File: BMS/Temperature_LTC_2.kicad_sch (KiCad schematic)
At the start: 35 parts, among them J15 Harwin M80-8542042

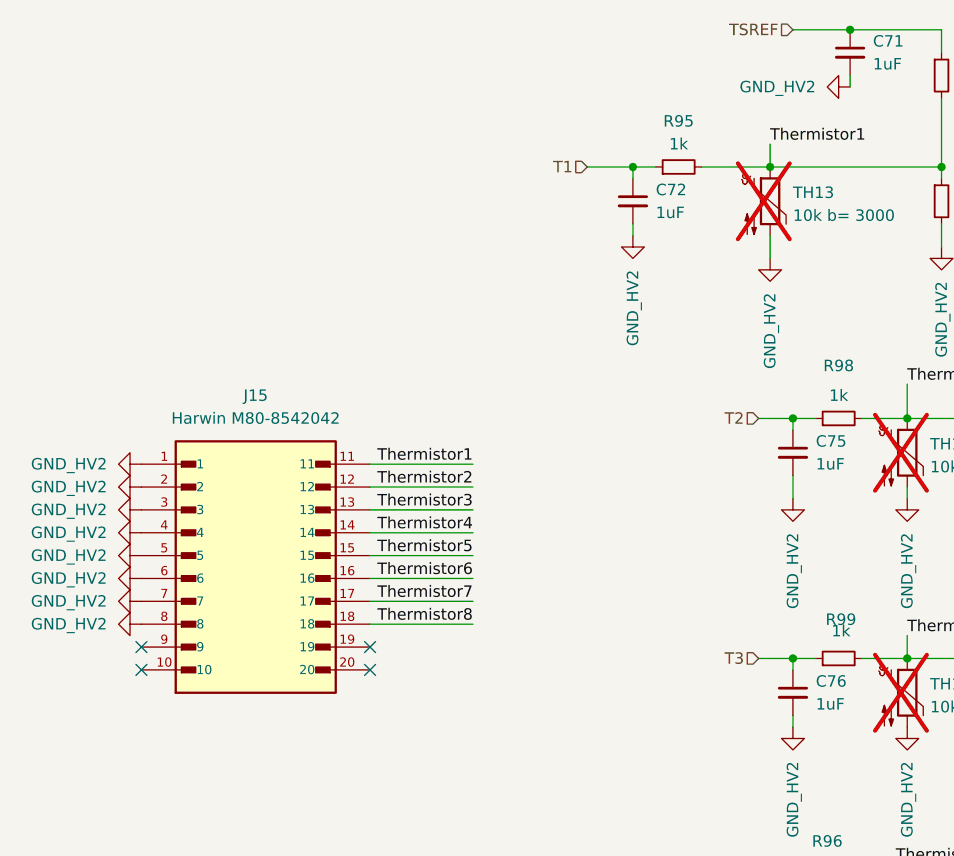
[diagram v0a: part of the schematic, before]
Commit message: Dodano layout drugiego bq79614, ukladu tlumaczącego z protokułu TI na UART oraz wstępnie poprowadzono pary różnicowe
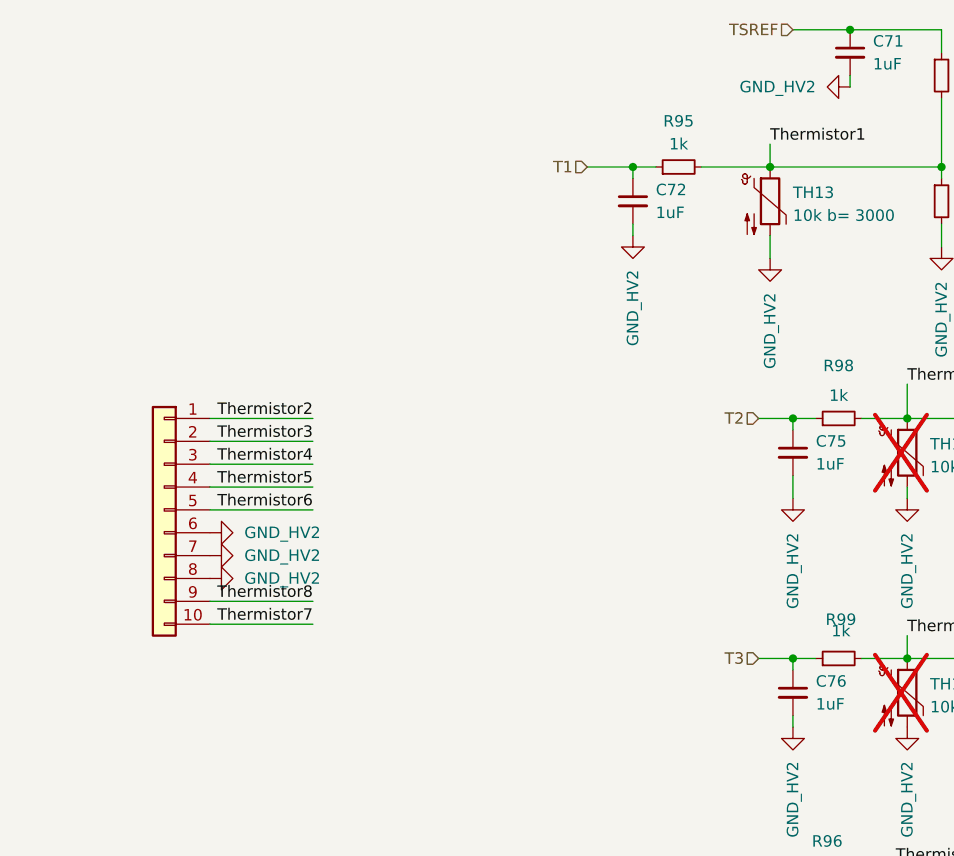
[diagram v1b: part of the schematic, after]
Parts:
- removed J15: Harwin M80-8542042, footrpint:HARWIN_M80-8542042, symbol M80-8542042:M80-8542042
- added J10: Conn_01x10, footrpint:HARWIN_G125-MV11005L1P, symbol Connector_Generic:Conn_01x10
- TH13: footprint (none) -> Resistor_SMD:R_0603_1608Metric_Pad0.98x0.95mm_HandSolder; now fitted; now in the parts list
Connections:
- net GND_HV2: now also J10.6 (Pin_6), J10.7 (Pin_7), J10.8 (Pin_8)
- net Thermistor2: now also J10.1 (Pin_1)
- net Thermistor3: now also J10.2 (Pin_2)
- net Thermistor4: now also J10.3 (Pin_3)
- net Thermistor5: now also J10.4 (Pin_4)
- net Thermistor6: now also J10.5 (Pin_5)
- net Thermistor7: now also J10.10 (Pin_10)
- net Thermistor8: now also J10.9 (Pin_9)
- no-connect marks 4 -> 0

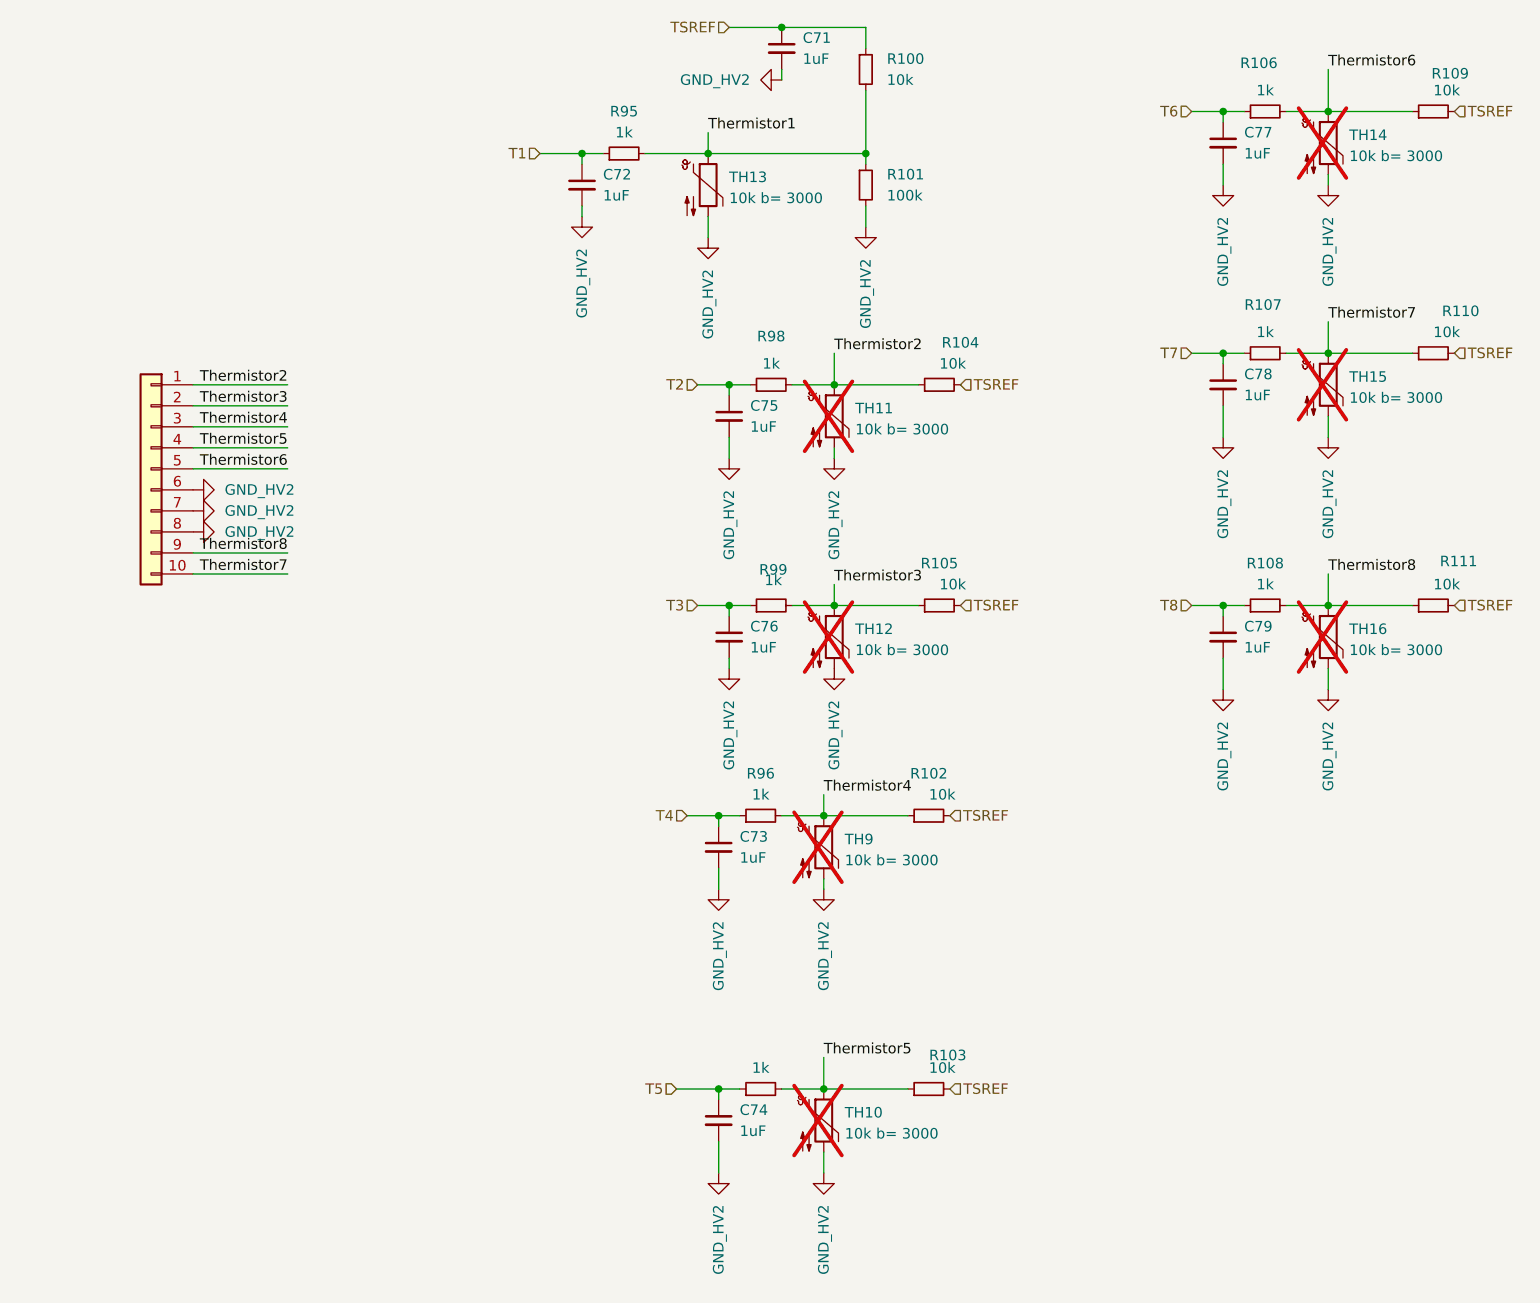
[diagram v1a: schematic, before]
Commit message: Iteracja 1.0 gotowa, teraz sprawdzenie i zmiany kosmetyczne
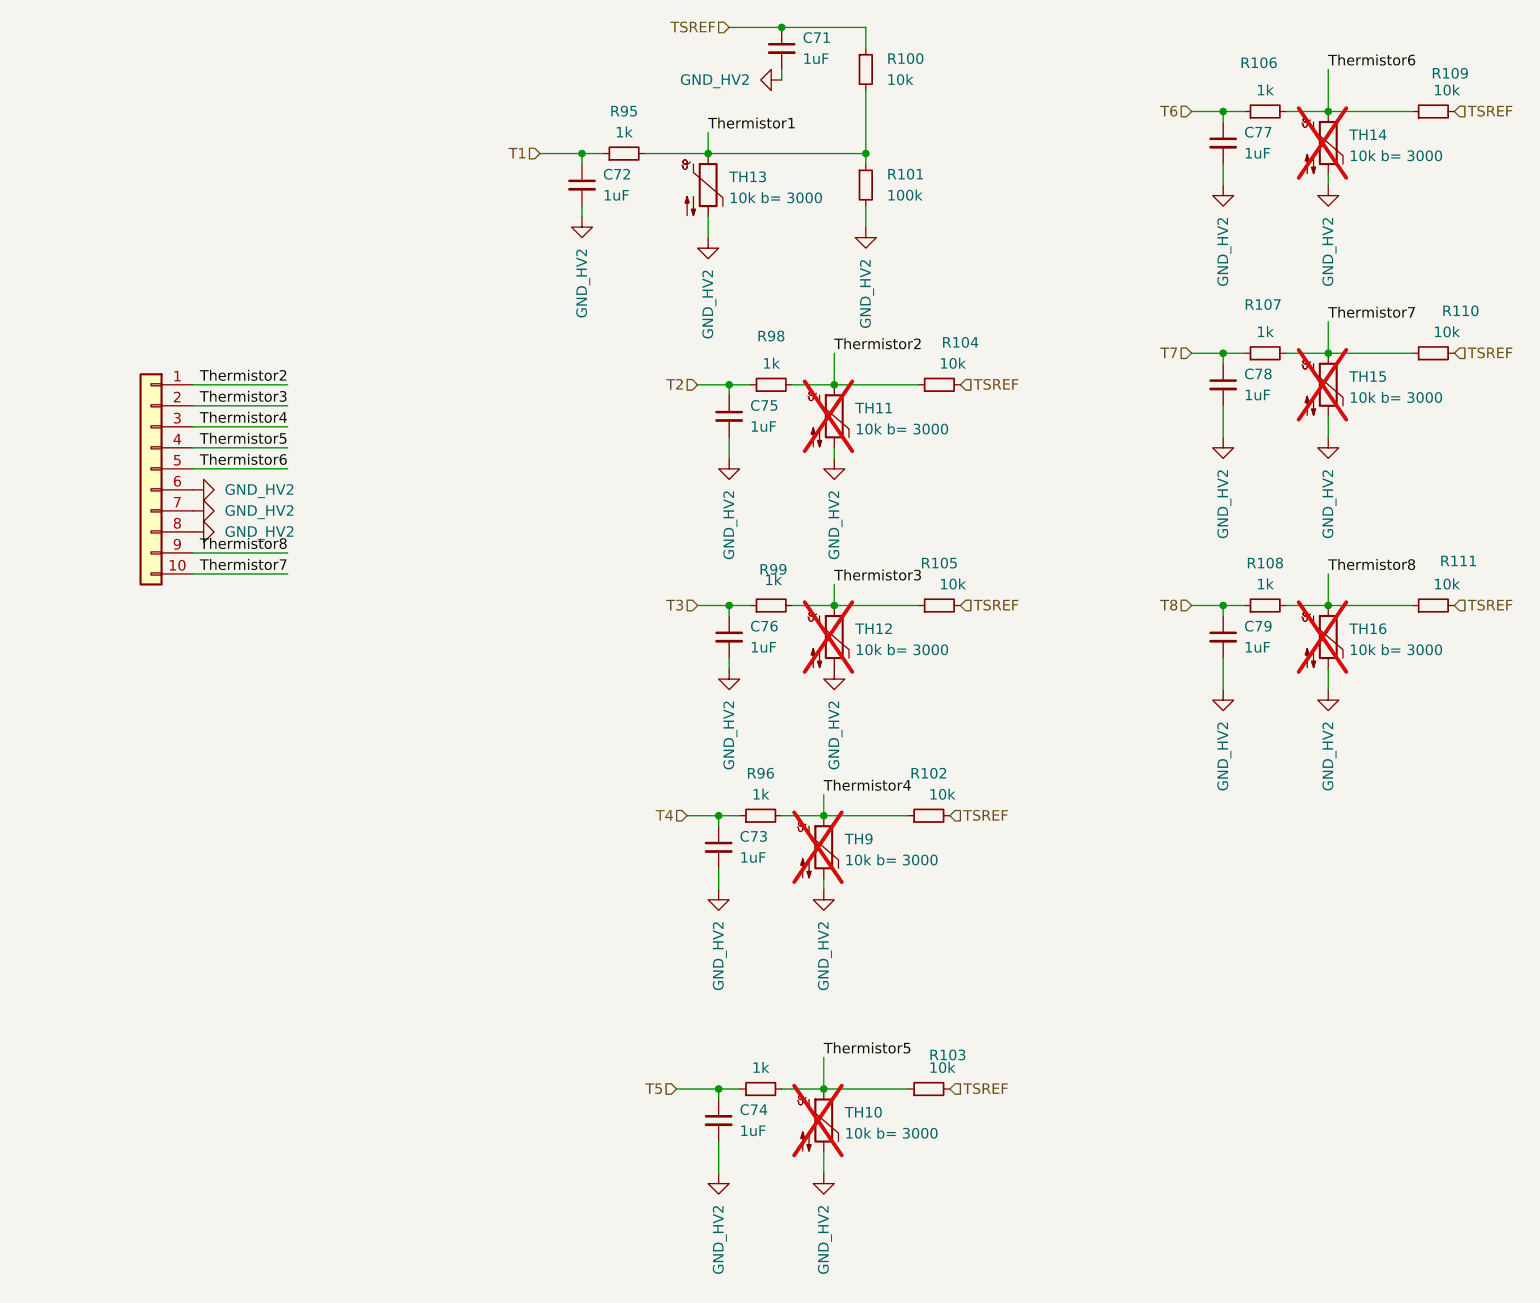
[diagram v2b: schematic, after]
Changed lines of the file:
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@@
 (kicad_sch
-	(version 20231120)
+	(version 20250114)
 	(generator "eeschema")
-	(generator_version "8.0")
+	(generator_version "9.0")
 	(paper "A4")
 	(junction
@@
 	(label "Thermistor7"
 		(at 181.61 55.88 0)
-		(fields_autoplaced yes)
 		(effects
 			(font
@@
 	(label "Thermistor3"
 		(at 55.88 66.04 180)
-		(fields_autoplaced yes)
 		(effects
 			(font
@@
 	(label "Thermistor8"
 		(at 181.61 86.36 0)
-		(fields_autoplaced yes)
 		(effects
 			(font
@@
 	(label "Thermistor5"
 		(at 55.88 71.12 180)
-		(fields_autoplaced yes)
 		(effects
 			(font
@@
 	(label "Thermistor2"
 		(at 121.92 59.69 0)
-		(fields_autoplaced yes)
 		(effects
 			(font
@@
 	(label "Thermistor6"
 		(at 181.61 25.4 0)
-		(fields_autoplaced yes)
 		(effects
 			(font
@@
 	(label "Thermistor5"
 		(at 120.65 144.78 0)
-		(fields_autoplaced yes)
 		(effects
 			(font
@@
 	(label "Thermistor6"
 		(at 55.88 73.66 180)
-		(fields_autoplaced yes)
 		(effects
 			(font
@@
 	(label "Thermistor8"
 		(at 55.88 83.82 180)
-		(fields_autoplaced yes)
 		(effects
 			(font
@@
 	(label "Thermistor4"
 		(at 55.88 68.58 180)
-		(fields_autoplaced yes)
 		(effects
 			(font
@@
 	(label "Thermistor2"
 		(at 55.88 63.5 180)
-		(fields_autoplaced yes)
 		(effects
 			(font
@@
 	(label "Thermistor4"
 		(at 120.65 113.03 0)
-		(fields_autoplaced yes)
 		(effects
 			(font
@@
 	(label "Thermistor3"
 		(at 121.92 87.63 0)
-		(fields_autoplaced yes)
 		(effects
 			(font
@@
 	(label "Thermistor7"
 		(at 55.88 86.36 180)
-		(fields_autoplaced yes)
 		(effects
 			(font
@@
 	(label "Thermistor1"
 		(at 106.68 33.02 0)
-		(fields_autoplaced yes)
 		(effects
 			(font
@@
 		(shape input)
 		(at 102.87 148.59 180)
-		(fields_autoplaced yes)
 		(effects
 			(font
@@
 		(shape input)
 		(at 109.22 20.32 180)
-		(fields_autoplaced yes)
 		(effects
 			(font
@@
 		(shape input)
 		(at 135.89 115.57 0)
-		(fields_autoplaced yes)
 		(effects
 			(font
@@
 		(shape input)
 		(at 104.14 115.57 180)
-		(fields_autoplaced yes)
 		(effects
 			(font
@@
 		(shape input)
 		(at 196.85 90.17 0)
-		(fields_autoplaced yes)
 		(effects
 			(font
@@
 		(shape input)
 		(at 137.16 63.5 0)
-		(fields_autoplaced yes)
 		(effects
 			(font
@@
 		(shape input)
 		(at 135.89 148.59 0)
-		(fields_autoplaced yes)
 		(effects
 			(font
@@
 		(shape input)
 		(at 105.41 90.17 180)
-		(fields_autoplaced yes)
 		(effects
 			(font
@@
 		(shape input)
 		(at 165.1 90.17 180)
-		(fields_autoplaced yes)
 		(effects
 			(font
@@
 		(shape input)
 		(at 165.1 30.48 180)
-		(fields_autoplaced yes)
 		(effects
 			(font
@@
 		(shape input)
 		(at 105.41 63.5 180)
-		(fields_autoplaced yes)
 		(effects
 			(font
@@
 		(shape input)
 		(at 165.1 59.69 180)
-		(fields_autoplaced yes)
 		(effects
 			(font
@@
 		(shape input)
 		(at 196.85 30.48 0)
-		(fields_autoplaced yes)
 		(effects
 			(font
@@
 		(shape input)
 		(at 86.36 35.56 180)
-		(fields_autoplaced yes)
 		(effects
 			(font
@@
 		(shape input)
 		(at 137.16 90.17 0)
-		(fields_autoplaced yes)
 		(effects
 			(font
@@
 		(shape input)
 		(at 196.85 59.69 0)
-		(fields_autoplaced yes)
-		(effects
-			(font
+		(effects
+			(font
